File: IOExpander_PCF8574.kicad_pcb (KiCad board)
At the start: 2 copper layers, 44.5 x 38.1 mm, 21 parts, among them J1 Conn_01x04_Pin, J2 Conn_01x08_Pin, J3 Conn_01x08_Pin, U1 PCF8574, U2 PCF8574

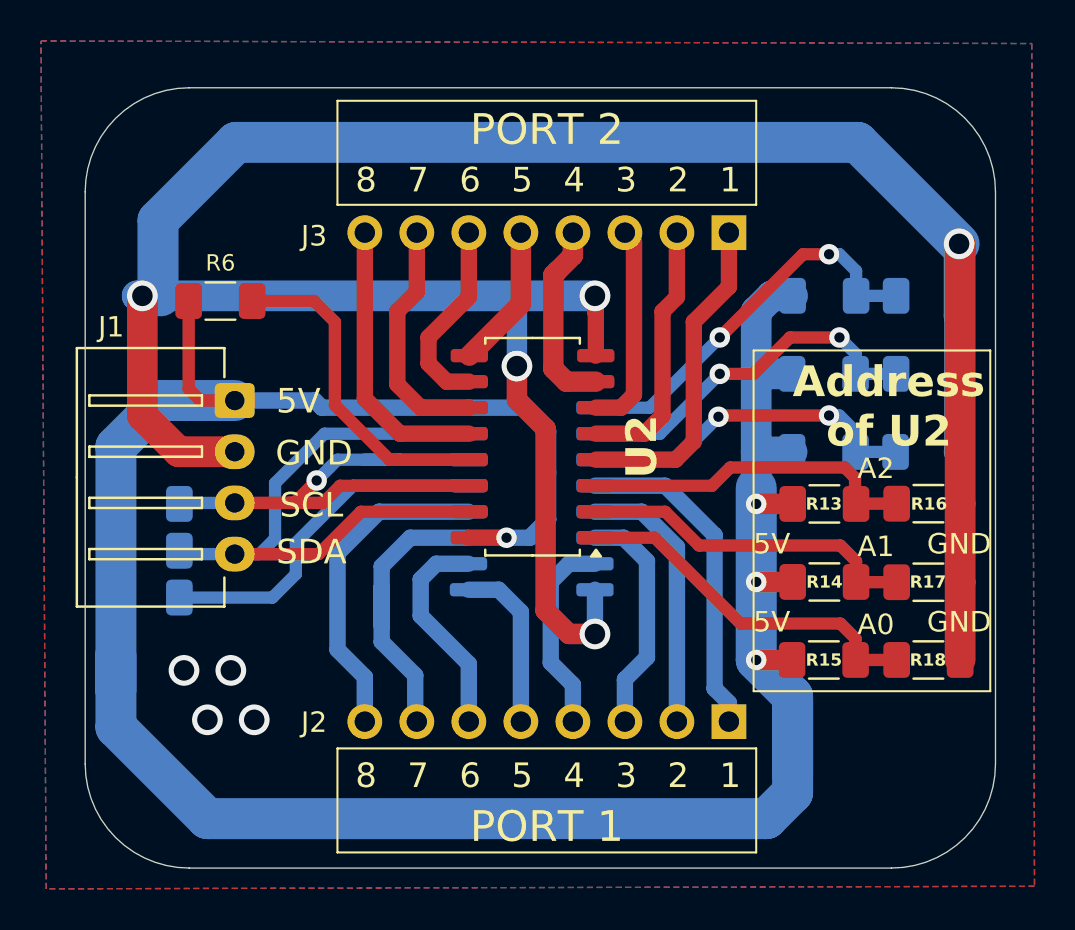
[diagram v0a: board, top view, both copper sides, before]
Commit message: Coupling Capacitors added
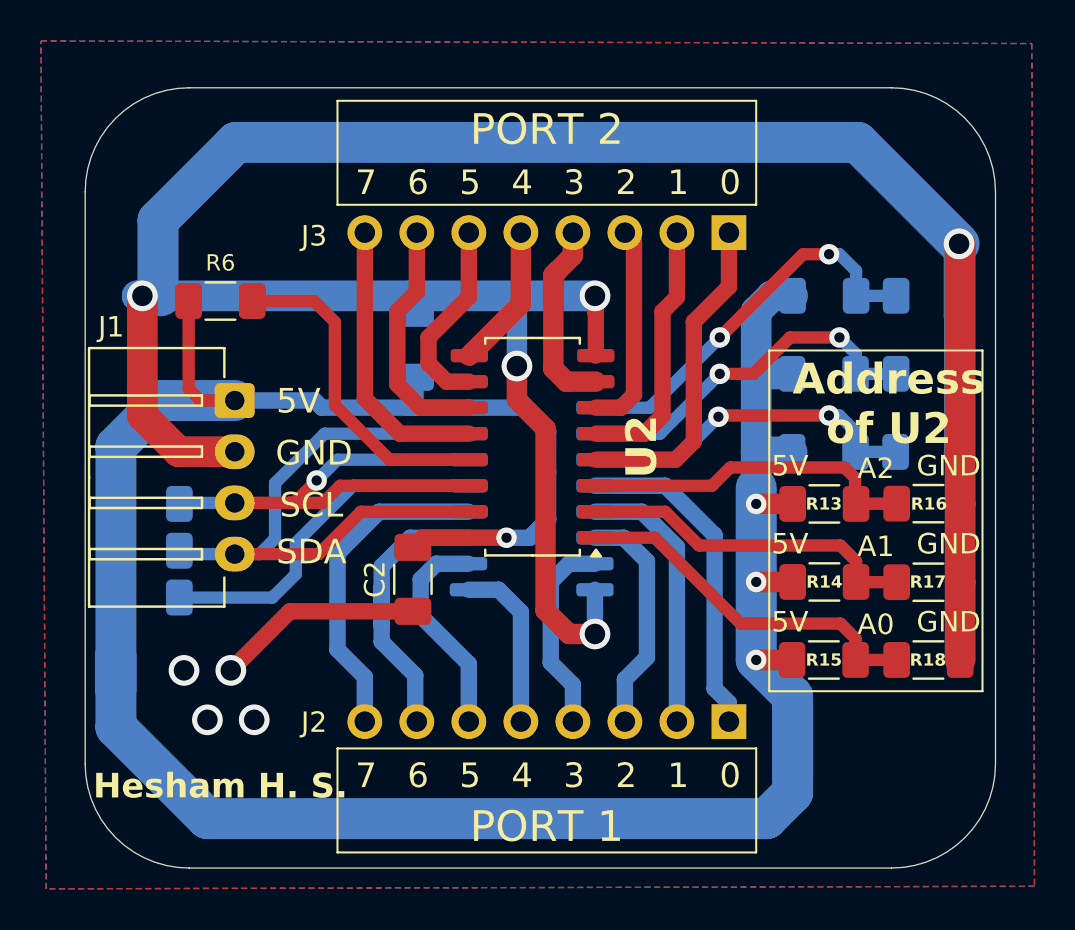
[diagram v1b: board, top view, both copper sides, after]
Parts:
- added C1: 0.1uF, Capacitor_SMD:C_1206_3216Metric_Pad1.33x1.80mm_HandSolder, B.Cu at (93.6, 46.9)
- added C2: 0.1uF, Capacitor_SMD:C_1206_3216Metric_Pad1.33x1.80mm_HandSolder, F.Cu at (93.5, 58.3)
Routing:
- net GND: track 135.7 -> 146.7 mm
- net 5V: track 158.5 -> 162.9 mm
- net /SDA: track 32.6 -> 30.5 mm
- net /SCL: track 30.8 -> 29.1 mm
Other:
- board text added: "0"
- board text added: "Hesham H. S."
- board text removed: "8"

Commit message: editing the footprint of PCF8574
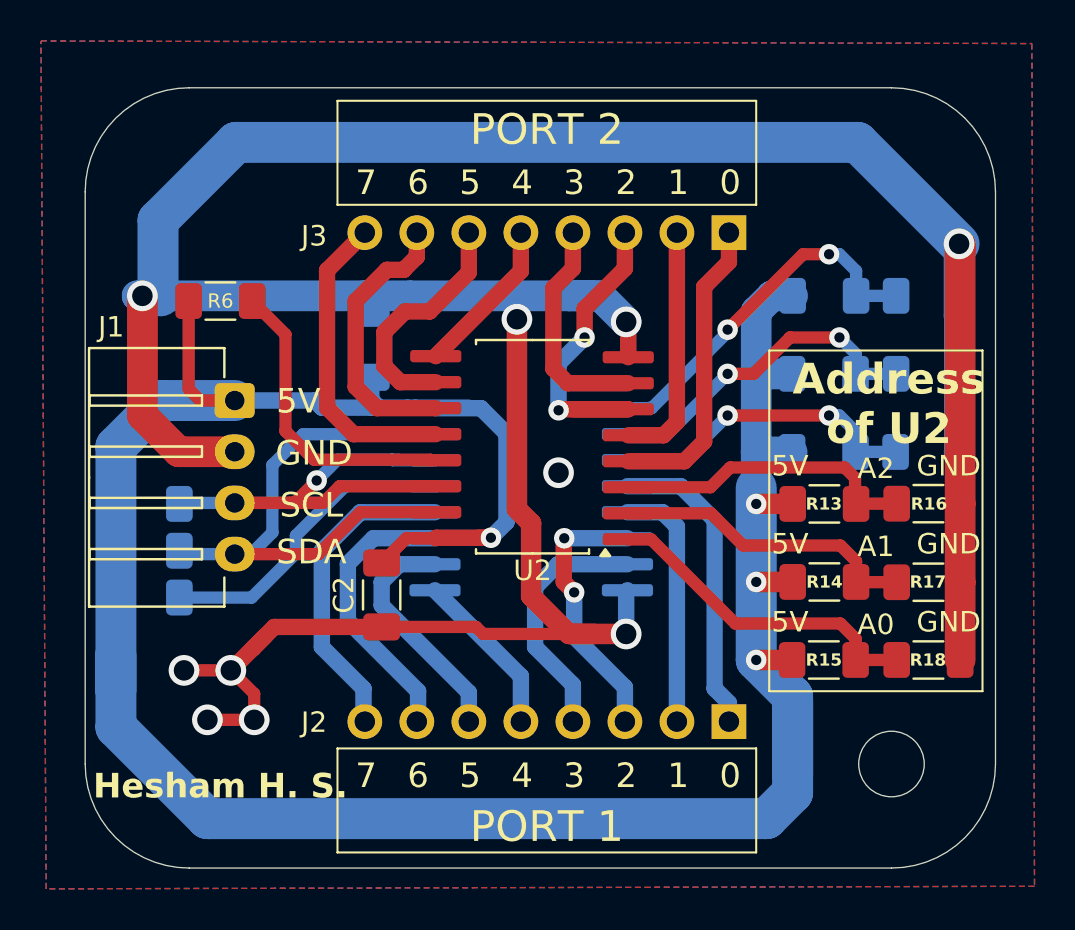
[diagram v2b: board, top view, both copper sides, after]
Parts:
- added REF**: MountingHole_3.2mm_M3, MountingHole:MountingHole_3.2mm_M3, F.Cu at (116.8, 67.3)
- U1, U2: footprint Package_SO:SOP-16_4.4x10.4mm_P1.27mm -> Package_SO:SO-16_5.3x10.2mm_P1.27mm
- moved C1 2.16 mm to (91.4, 46.9)
- moved C2 1.70 mm to (91.9, 59.1)
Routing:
- net GND: track 146.7 -> 169.9 mm, vias 9 -> 10
- net Net-(J3-Pin_3): track 10.2 -> 16.2 mm, vias 0 -> 2
- net /SDA: track 30.5 -> 27.6 mm
- net /SCL: track 29.1 -> 26.2 mm
- net Net-(J2-Pin_4): track 9.80 -> 12.3 mm
- net Net-(J3-Pin_6): track 9.56 -> 11.8 mm
- net Net-(U1-~{INT}): track 17.3 -> 15.2 mm
- net Net-(J2-Pin_3): track 11.3 -> 13.3 mm, vias 0 -> 2
- net Net-(J3-Pin_7): track 11.8 -> 13.6 mm
- net /1_A2: track 17.0 -> 15.3 mm
- net /2_A0: track 17.8 -> 16.2 mm
- net /2_A1: track 16.7 -> 15.1 mm
- net Net-(J3-Pin_4): track 9.37 -> 11.0 mm
- net /1_A1: track 18.0 -> 16.4 mm
- net /2_A2: track 16.5 -> 15.0 mm
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
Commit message: Pull Up resistors are added for each channel
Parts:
- added R19: 4.7k, Resistor_SMD:R_1206_3216Metric_Pad1.30x1.75mm_HandSolder, B.Cu at (103.8, 37.0)
- added R20: 4.7k, Resistor_SMD:R_1206_3216Metric_Pad1.30x1.75mm_HandSolder, B.Cu at (101.3, 37.0)
- added R21: 4.7k, Resistor_SMD:R_1206_3216Metric_Pad1.30x1.75mm_HandSolder, B.Cu at (98.8, 37.0)
- added R22: 4.7k, Resistor_SMD:R_1206_3216Metric_Pad1.30x1.75mm_HandSolder, B.Cu at (96.2, 37.0)
- added R23: 4.7k, Resistor_SMD:R_1206_3216Metric_Pad1.30x1.75mm_HandSolder, B.Cu at (93.7, 37.0)
- added R24: 4.7k, Resistor_SMD:R_1206_3216Metric_Pad1.30x1.75mm_HandSolder, B.Cu at (91.1, 37.0)
- added R25: 4.7k, Resistor_SMD:R_1206_3216Metric_Pad1.30x1.75mm_HandSolder, B.Cu at (108.9, 69.6)
- added R26: 4.7k, Resistor_SMD:R_1206_3216Metric_Pad1.30x1.75mm_HandSolder, B.Cu at (106.4, 69.6)
- added R27: 4.7k, Resistor_SMD:R_1206_3216Metric_Pad1.30x1.75mm_HandSolder, B.Cu at (103.8, 69.6)
- added R28: 4.7k, Resistor_SMD:R_1206_3216Metric_Pad1.30x1.75mm_HandSolder, B.Cu at (101.3, 69.6)
- added R29: 4.7k, Resistor_SMD:R_1206_3216Metric_Pad1.30x1.75mm_HandSolder, B.Cu at (98.8, 69.6)
- added R30: 4.7k, Resistor_SMD:R_1206_3216Metric_Pad1.30x1.75mm_HandSolder, B.Cu at (96.2, 69.6)
- added R31: 4.7k, Resistor_SMD:R_1206_3216Metric_Pad1.30x1.75mm_HandSolder, B.Cu at (93.7, 69.6)
- added R32: 4.7k, Resistor_SMD:R_1206_3216Metric_Pad1.30x1.75mm_HandSolder, B.Cu at (91.1, 69.6)
- added R4: 4.7k, Resistor_SMD:R_1206_3216Metric_Pad1.30x1.75mm_HandSolder, B.Cu at (108.9, 37.0)
- added R5: 4.7k, Resistor_SMD:R_1206_3216Metric_Pad1.30x1.75mm_HandSolder, B.Cu at (106.4, 37.0)
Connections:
- net Net-(J2-Pin_1) renamed /P00
- net Net-(J2-Pin_2) renamed /P01
- net Net-(J2-Pin_3) renamed /P02
- net Net-(J2-Pin_4) renamed /P03
- net Net-(J2-Pin_5) renamed /P04
- net Net-(J2-Pin_6) renamed /P05
- net Net-(J2-Pin_7) renamed /P06
- net Net-(J2-Pin_8) renamed /P07
- net Net-(J3-Pin_1) renamed /P10
- net Net-(J3-Pin_2) renamed /P11
- net Net-(J3-Pin_3) renamed /P12
- net Net-(J3-Pin_4) renamed /P13
- net Net-(J3-Pin_5) renamed /P14
- net Net-(J3-Pin_6) renamed /P15
- net Net-(J3-Pin_7) renamed /P16
- net Net-(J3-Pin_8) renamed /P17
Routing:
- net 5V: track 164.1 -> 183.2 mm
- net /P12: track 16.2 -> 19.0 mm
- net /P10: track 14.8 -> 17.6 mm
- net /P15: track 11.8 -> 14.6 mm
- net /P14: track 7.75 -> 10.6 mm
- net /P11: track 11.9 -> 14.7 mm
- net /P17: track 15.2 -> 18.0 mm
- net /P16: track 13.6 -> 16.4 mm
- net /P13: track 11.0 -> 13.8 mm
- net /P07: track 15.5 -> 18.3 mm
- net /P06: track 13.9 -> 16.7 mm
- net /P05: track 11.5 -> 14.4 mm
- net /P04: track 8.15 -> 11.0 mm
- net /P01: track 12.2 -> 15.0 mm
- net /P00: track 15.1 -> 17.9 mm
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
